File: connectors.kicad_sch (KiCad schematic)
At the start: 4 parts, among them J1 Conn_01x04_Pin, J2 Conn_01x04_Pin, J3 Conn_01x09_Pin, J4 Conn_02x03_Odd_Even

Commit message: Completed symbol-footprint associations.
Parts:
- J1, J2: footprint (none) -> Connector_PinHeader_2.54mm:PinHeader_1x04_P2.54mm_Vertical
- J3: footprint (none) -> Connector_PinHeader_2.54mm:PinHeader_1x09_P2.54mm_Vertical
- J4: footprint (none) -> Connector_PinHeader_2.54mm:PinHeader_2x03_P2.54mm_Vertical
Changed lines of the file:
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@@
 			)
 		)
-		(property "Footprint" ""
+		(property "Footprint" "Connector_PinHeader_2.54mm:PinHeader_1x09_P2.54mm_Vertical"
 			(at 92.71 95.25 0)
 			(effects
@@
 			)
 		)
-		(property "Footprint" ""
+		(property "Footprint" "Connector_PinHeader_2.54mm:PinHeader_1x04_P2.54mm_Vertical"
 			(at 92.71 64.77 0)
 			(effects
@@
 			)
 		)
-		(property "Footprint" ""
+		(property "Footprint" "Connector_PinHeader_2.54mm:PinHeader_1x04_P2.54mm_Vertical"
 			(at 116.84 64.77 0)
 			(effects
@@
 			)
 		)
-		(property "Footprint" ""
+		(property "Footprint" "Connector_PinHeader_2.54mm:PinHeader_2x03_P2.54mm_Vertical"
 			(at 118.11 92.71 0)
 			(effects

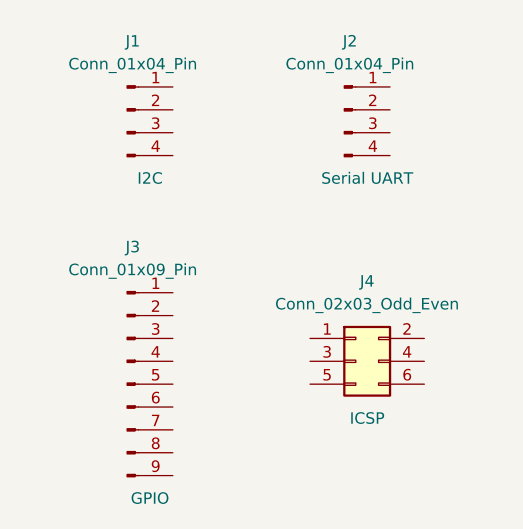
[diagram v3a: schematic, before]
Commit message: Completed wiring and ERC. Fixed some issues.
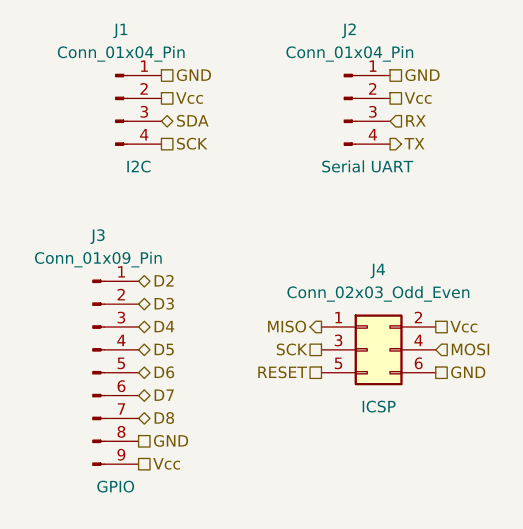
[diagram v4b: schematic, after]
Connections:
- net D2: now reaches J3.1 (Pin_1)
- net D3: now reaches J3.2 (Pin_2)
- net D4: now reaches J3.3 (Pin_3)
- net D5: now reaches J3.4 (Pin_4)
- net D6: now reaches J3.5 (Pin_5)
- net D7: now reaches J3.6 (Pin_6)
- net D8: now reaches J3.7 (Pin_7)
- net GND: now reaches J3.8 (Pin_8)
- net GND: now also J1.1 (Pin_1), J2.1 (Pin_1), J4.6 (Pin_6)
- net Vcc: now reaches J3.9 (Pin_9)
- net Vcc: now also J1.2 (Pin_2), J2.2 (Pin_2), J4.2 (Pin_2)
- net SDA: now reaches J1.3 (Pin_3)
- net SCK: now reaches J1.4 (Pin_4)
- net SCK: now also J4.3 (Pin_3)
- net RX: now reaches J2.3 (Pin_3)
- net TX: now reaches J2.4 (Pin_4)
- net MISO: now reaches J4.1 (Pin_1)
- net MOSI: now reaches J4.4 (Pin_4)
- net RESET: now reaches J4.5 (Pin_5)
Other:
- moved on the sheet: J1, J2, J3, J4

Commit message: Fixed defects relating to SCL/SCK confusion.
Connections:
- net SCK: no longer J1.4 (Pin_4)
- new net SCL: J1.4 (Pin_4)
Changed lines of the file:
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@@
 		)
 	)
-	(hierarchical_label "SCK"
+	(hierarchical_label "SCL"
 		(shape passive)
 		(at 96.52 68.58 0)
